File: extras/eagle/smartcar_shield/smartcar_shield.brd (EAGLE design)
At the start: 49.7 x 53.2 mm, 22 parts, among them IC1 L293D, J1 ARDUINO_R3_SHIELD

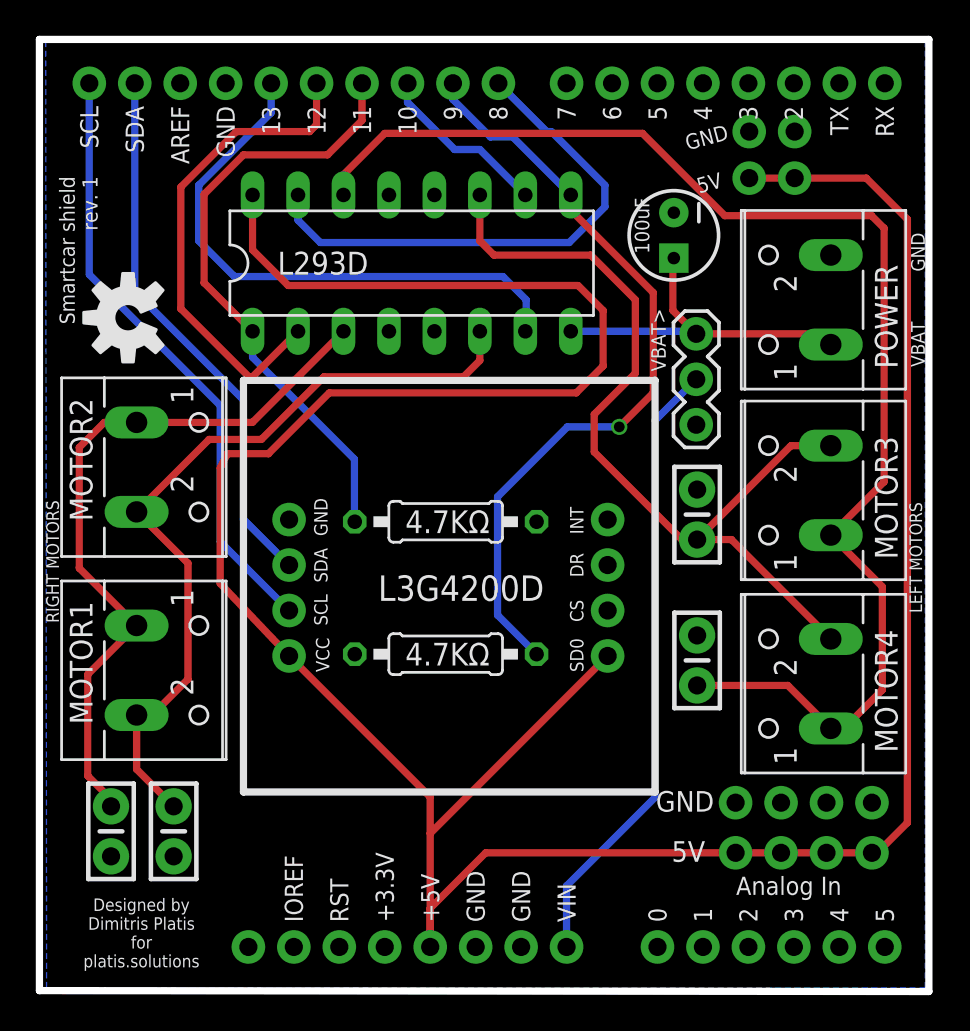
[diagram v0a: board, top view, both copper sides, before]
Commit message: Update board to rev. 2
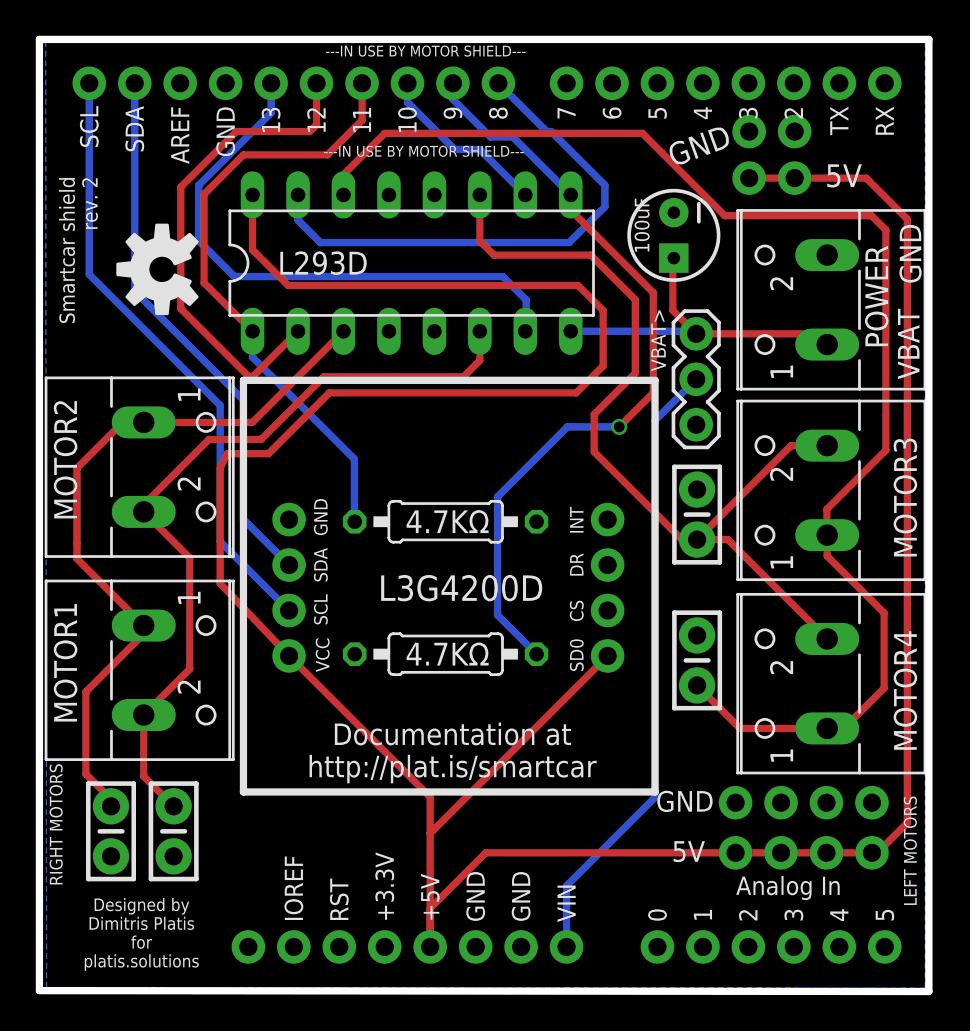
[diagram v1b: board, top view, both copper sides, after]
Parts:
- moved U$1 3.30 mm to (6.35, 40.4)
- moved MOTOR1 0.40 mm to (6.60, 18.0)
- moved MOTOR2 0.40 mm to (6.60, 29.4)
- moved MOTOR3 0.20 mm to (42.2, 28.1)
- moved MOTOR4 0.20 mm to (42.2, 17.2)
- moved POWER 0.20 mm to (42.2, 38.7)
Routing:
- net MOTORA-OUT2: track 44.5 -> 43.4 mm
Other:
- board text added: "---IN USE BY MOTOR SHIELD---"
- board text added: "Documentation at http://plat.is/smartcar"
- board text added: "Smartcar shield rev. 2"
- board text removed: "Find documentation at http://plat.is/smartcar"
- board text removed: "GND 5V"
- board text removed: "Smartcar shield rev. 1"
